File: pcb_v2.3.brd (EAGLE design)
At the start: 19.4 x 108.4 mm, 57 parts, among them J1 PJ301_THONKICONN6, J2 PJ301_THONKICONN6, J3 PJ301_THONKICONN6, J4 PJ301_THONKICONN6, U1 MCP6004, U2 TL074_SMD, U5 TL074

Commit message: new board layout
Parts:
- moved R24 77.5 mm to (10.4, 93.0), turned to 90 degrees
- moved R18 71.4 mm to (10.4, 87.6), turned to 270 degrees
- moved R19 37.2 mm to (9.91, 32.5), turned to 180 degrees
- moved R22 35.4 mm to (9.91, 30.2)
- moved R20 29.5 mm to (2.03, 3.81), turned to 270 degrees
- moved R34 29.3 mm to (11.9, 3.81), turned to 270 degrees
- moved R14 29.1 mm to (2.54, 9.40), turned to 180 degrees
- moved R35 28.7 mm to (12.4, 1.02)
- moved R28 27.8 mm to (8.13, 1.02)
- moved R36 27.5 mm to (18.3, 1.02), turned to 180 degrees
- moved R16 25.5 mm to (9.91, 24.9)
- moved R13 24.7 mm to (9.91, 27.2)
- moved R21 23.9 mm to (18.3, 9.40)
- moved U$1 0.51 mm to (6.10, 94.5)
- moved R27 0.25 mm to (2.54, 1.02)
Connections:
- net N$14 renamed HIGH_SUM_FDBK
- net N$19 renamed MOD_SUM_FDBK
- net N$4 renamed LOW_SUM_FDBK
- net N$9 renamed MID_SUM_FDBK
- net N$1: no longer U2.2
- net N$10: no longer U2.3
- net N$13: now also U2.1; no longer U2.8
- net N$3: no longer U2.1
- net N$6: now also U2.2; no longer U2.9
- net N$7: now also U2.3; no longer U2.10

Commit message: route board
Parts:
- removed C1, C2, C3, C4: 100n, rcl:C0603
- moved R6 65.1 mm to (18.0, 94.7)
- moved R12 57.5 mm to (18.0, 83.1)
- moved R11 52.9 mm to (11.4, 98.3)
- moved R5 52.9 mm to (9.14, 98.3)
- moved R17 51.4 mm to (9.14, 94.7)
- moved R23 51.4 mm to (11.4, 94.7)
- moved R2 31.4 mm to (2.54, 16.3), turned to 180 degrees
- moved R29 31.4 mm to (2.54, 13.7)
- moved R32 30.1 mm to (18.3, 14.0)
- moved R26 29.9 mm to (11.4, 20.3), turned to 180 degrees
- moved R31 29.9 mm to (11.4, 17.8)
- moved R9 27.2 mm to (11.4, 22.6)
- moved R3 26.6 mm to (2.54, 22.4), turned to 180 degrees
- moved R10 26.1 mm to (18.3, 39.1)
- moved R7 26.1 mm to (18.3, 41.4)
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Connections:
- net MOD_SUM_FDBK renamed MOD_SUM_OUT
- net N$15 renamed MOD_ATNV_FDBK
- net N$6 renamed HIGH_ATNV_FDBK
- net SV2_2 renamed NC
- removed net HIGH_SUM_FDBK: R13.1, R16.2, U5.8
- removed net LOW_SUM_FDBK: R1.1, R4.2, U5.1
- removed net MID_SUM_FDBK: R10.2, R7.1, U5.7
- removed net N$10: LOW_ATNV.P$2
- removed net N$11: MID_ATNV.P$2, U2.5
- removed net N$16: U$1.P$4
- removed net N$2 (its old number): R26.1, R31.2, U2.6
- removed net N$31: R3.2, R30.2, R4.1, U5.2
- new net HIGH_SUM_OUT: R13.1, R16.2, U5.1
- new net LOW_ATNV_FDBK: R2.1, R29.2, U2.6
- new net LOW_SUM_OUT: R1.1, R4.2, U5.7
- new net MID_ATNV_FDBK: R26.1, R31.2, U2.9
- new net MID_SUM_OUT: R10.2, R7.1, U5.8
- new net N$4: LOW_ATNV.P$2, U2.5
- new net N$6: R3.2, R30.2, R4.1, U5.6
- net 3V: now also U$1.P$4
- net GND: no longer C1.2, C2.2, C3.2, C4.2
- net HIGH_OUT: no longer C3.1
- net LOW_OUT: no longer C1.1
- net MID_OUT: no longer C2.1
- net MOD_OUT: no longer C4.1
- net N$1: now also MID_ATNV.P$2, U2.10; no longer R2.1, R29.2
- net N$3: now also U2.7
- net N$33: now also U2.8; no longer U2.7
- net N$37: now also U5.2; no longer U5.9
- net N$8: now also U5.9; no longer U5.6
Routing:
- net HIGH_IN: track 0.00 -> 110.0 mm, vias 0 -> 7
- net MID_IN: track 0.00 -> 107.6 mm, vias 0 -> 5
- net MOD_IN: track 0.00 -> 104.6 mm, vias 0 -> 6
- net LOW_IN: track 0.00 -> 98.8 mm, vias 0 -> 5
- net N$23: track 0.00 -> 76.5 mm, vias 0 -> 7
- net N$2: track 0.00 -> 74.5 mm, vias 0 -> 4
- net N$24: track 0.00 -> 73.3 mm, vias 0 -> 4
- net N$30: track 0.00 -> 72.9 mm, vias 0 -> 2
- net N$4: track 0.00 -> 71.6 mm, vias 0 -> 2
- net N$12: track 0.00 -> 69.1 mm, vias 0 -> 1
- net 12V: track 0.00 -> 67.8 mm, vias 0 -> 8
- net SW_HIGH: track 0.00 -> 59.5 mm, vias 0 -> 3
- net N$32: track 0.00 -> 57.7 mm, vias 0 -> 4
- net N$1: track 0.00 -> 57.6 mm, vias 0 -> 5
- net N$26: track 0.00 -> 54.4 mm
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
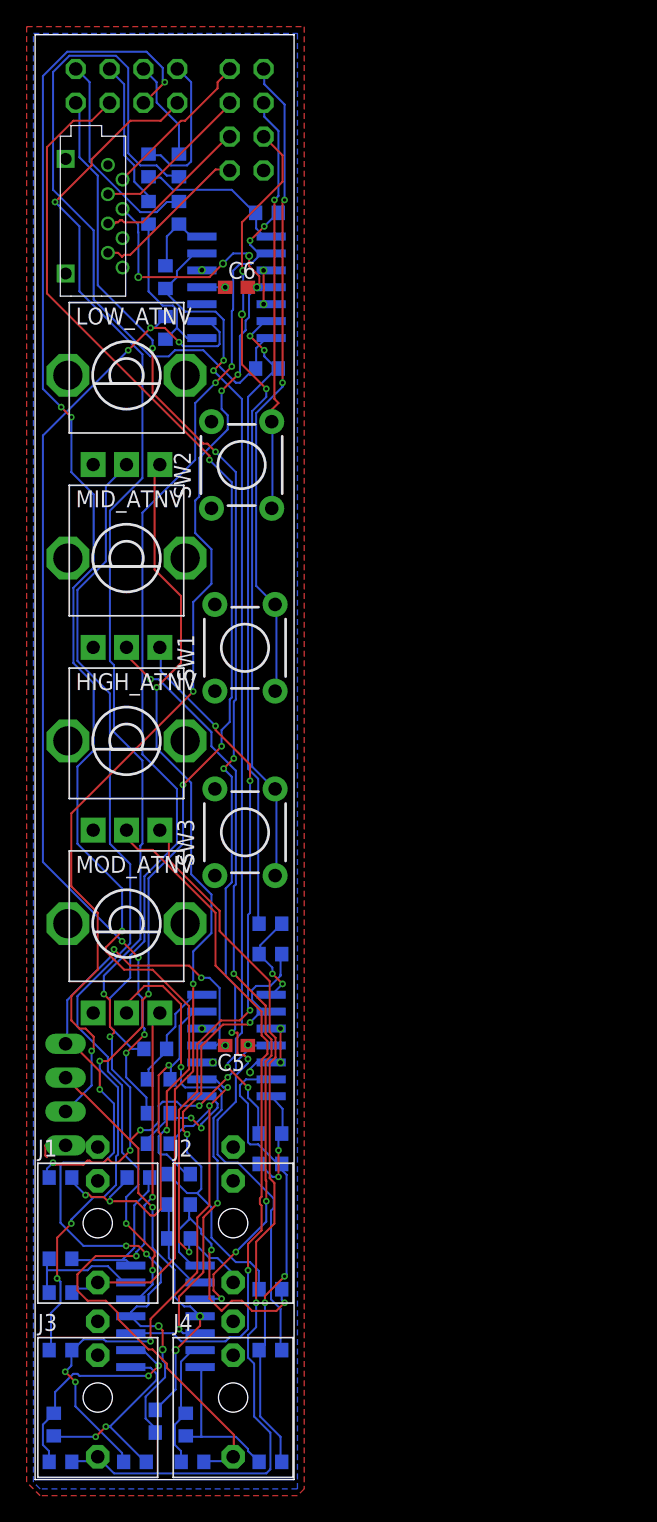
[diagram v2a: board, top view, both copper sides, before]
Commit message: fix switch ordering
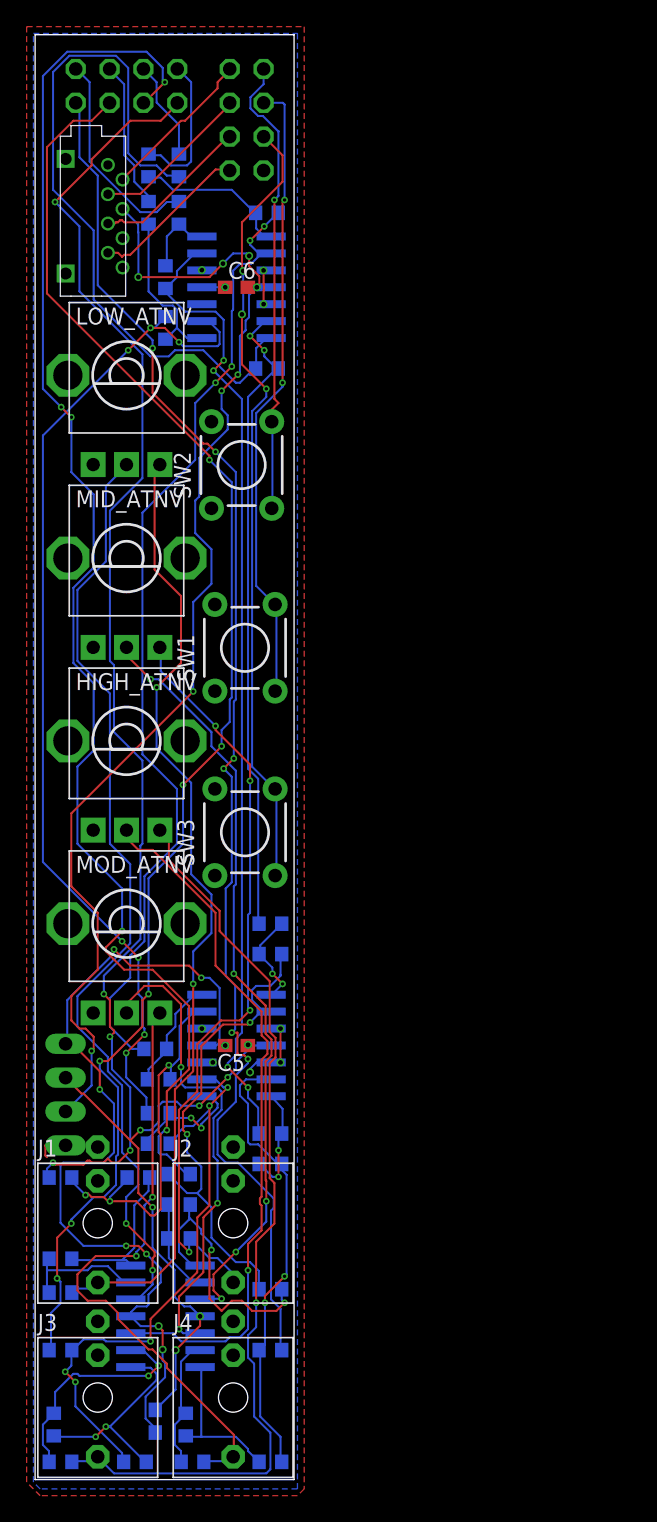
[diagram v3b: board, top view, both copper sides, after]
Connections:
- net SW_LOW: now also SW2.3, SW2.4; no longer SW1.3, SW1.4
- net SW_MID: now also SW1.3, SW1.4; no longer SW2.3, SW2.4
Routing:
- net SW_MID: track 31.4 -> 47.2 mm, vias 1 -> 2
- net SW_LOW: track 48.9 -> 35.0 mm, vias 2 -> 1
